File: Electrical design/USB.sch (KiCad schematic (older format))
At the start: 18 parts, among them P501 USB_OTG, Q501 Q_NMOS_GSD, Q502 Q_PMOS_GSD, U501 TPD2E001, U502 MCP73834

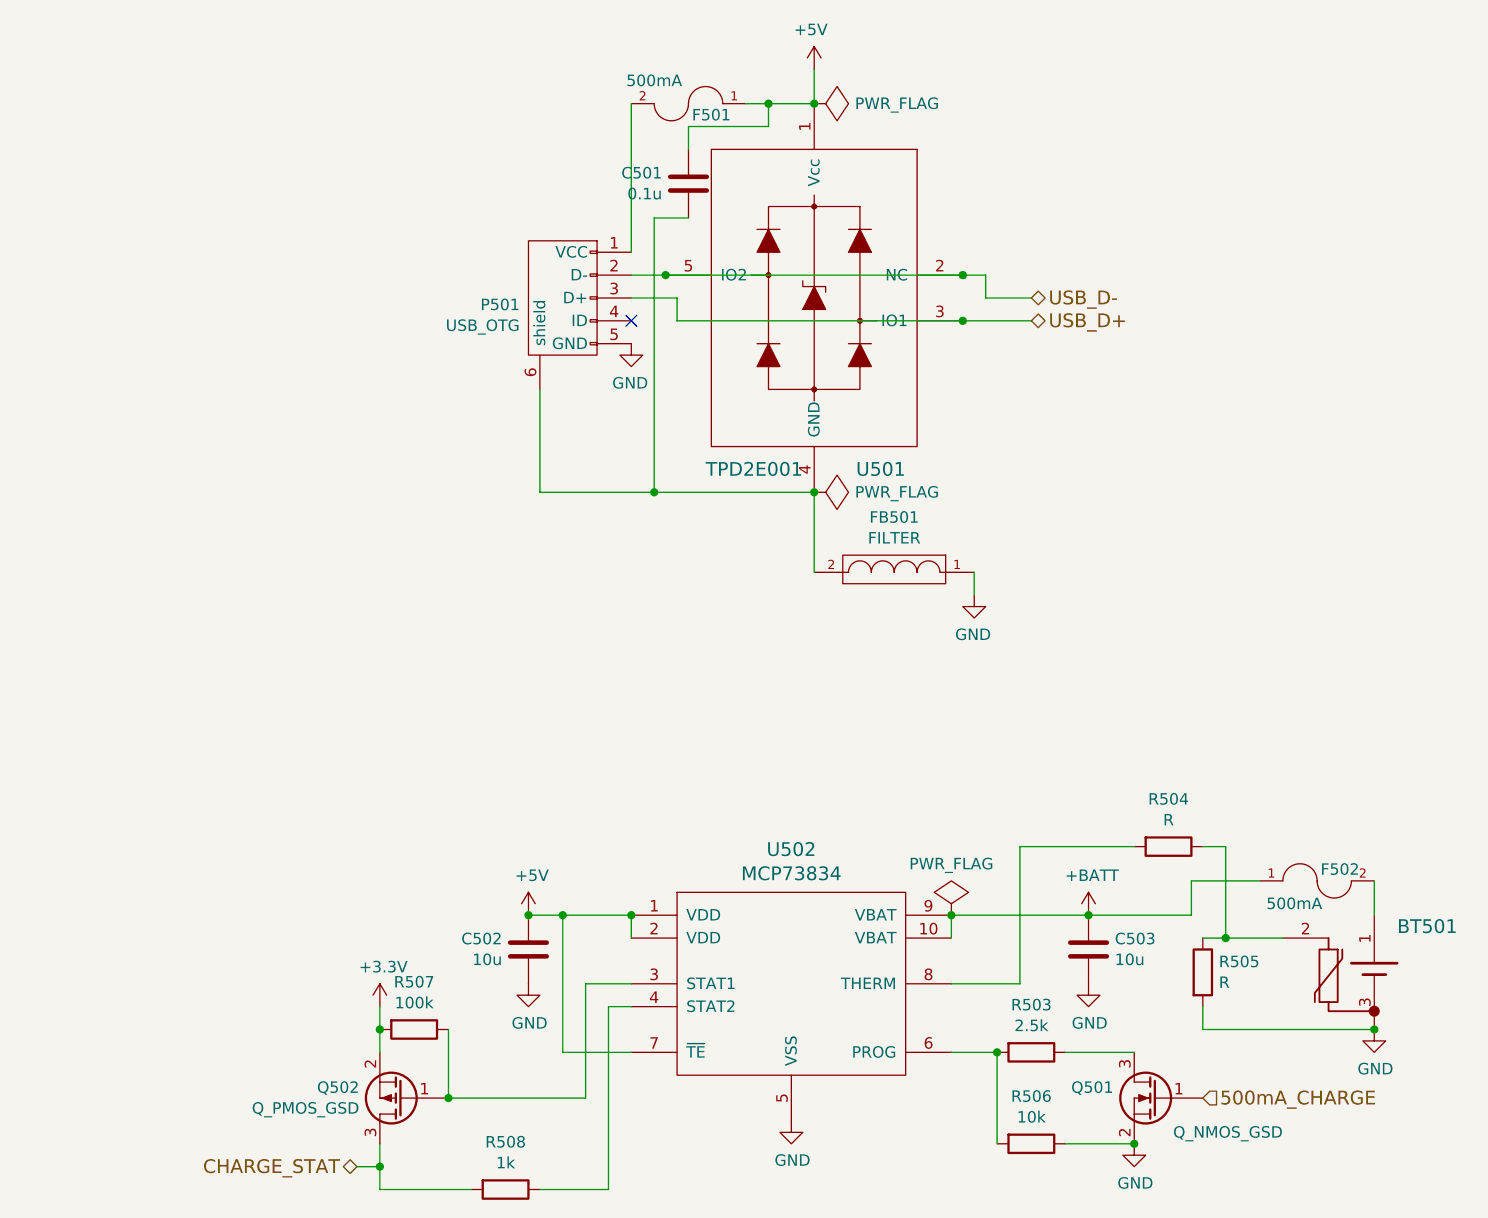
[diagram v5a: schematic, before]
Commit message: Add documentation. Fix some issues found while writing it.
The issues fixed:
Change R245-246 to 1M.
Remove D211-212 and add D213-214.
Power the analog switches from +V_int.
Reconfigure range combination jumpers.
Remove "GND" net.
Correct values of C103-105, and add R106-108 (correcting values of R101-103).
Change +V_int around to be based of +3.3VA instead of +BATT, and clamp to 3.5 V.
Along with above, remove GND rail, mostly replacing with GNDA.
Update PCB for changes.
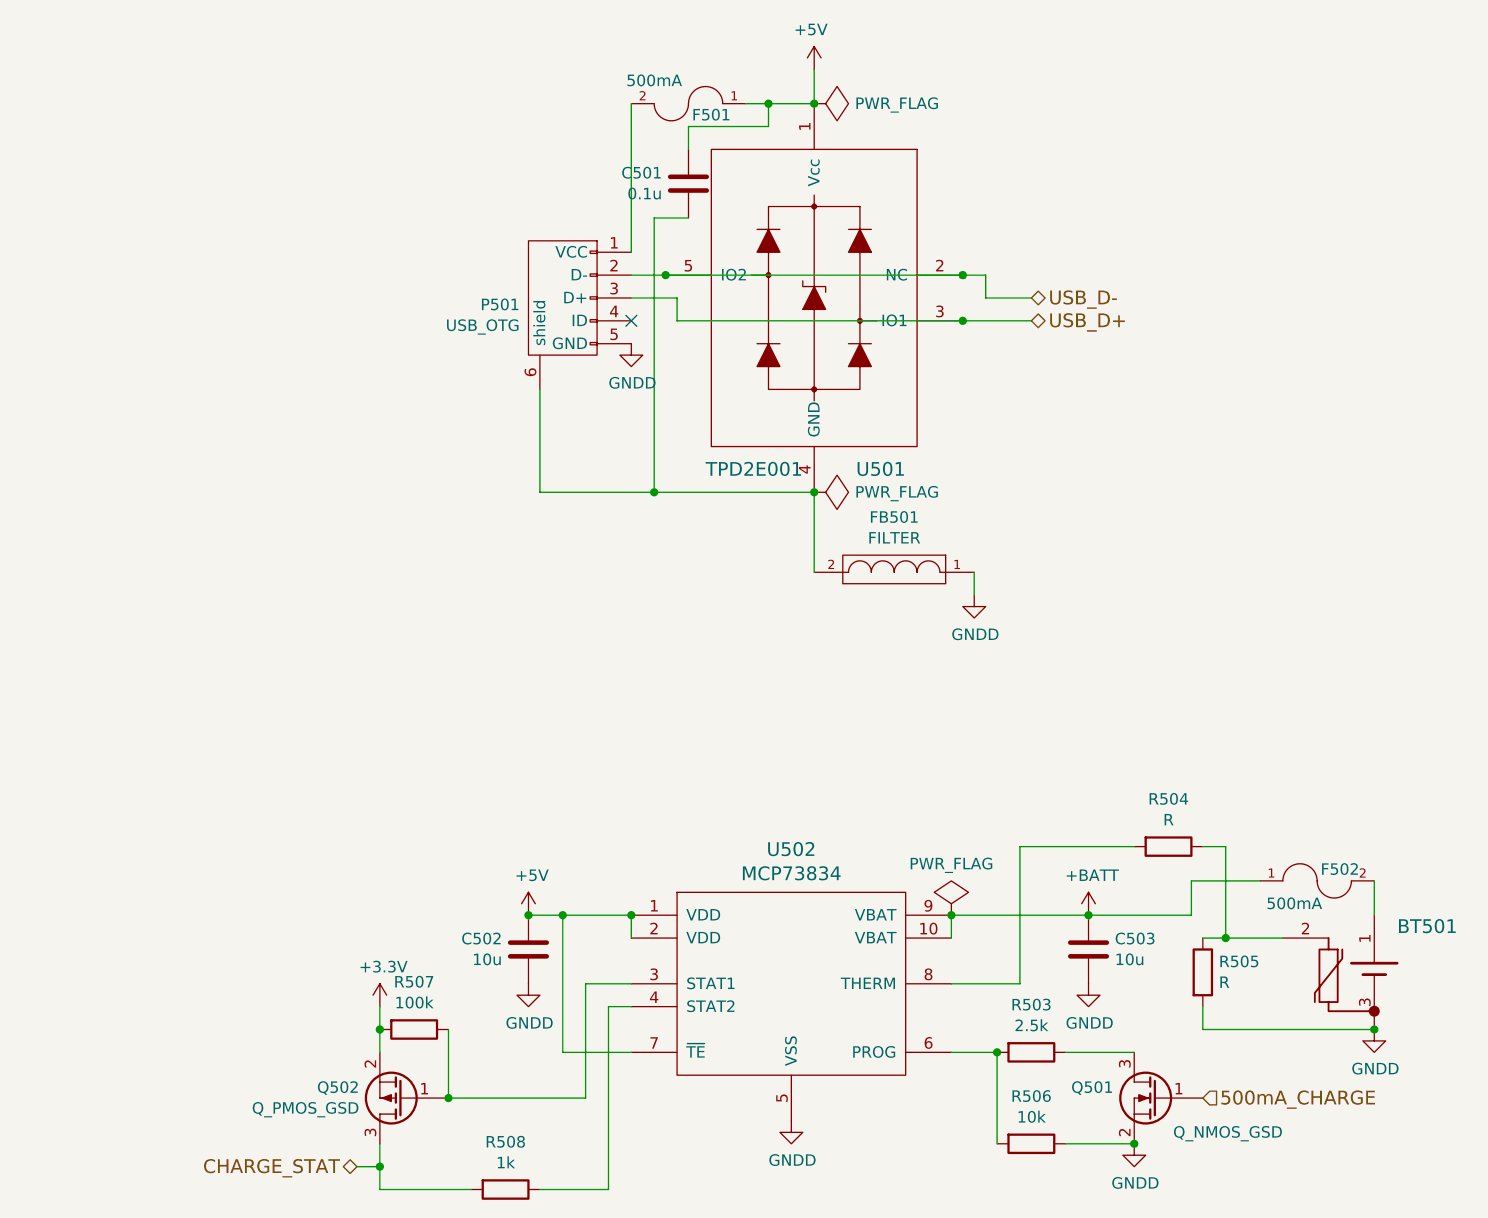
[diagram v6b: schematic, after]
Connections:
- net GND renamed GNDD
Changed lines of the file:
@@
 Sheet 5 5
 Title "USB and charging"
-Date "2016-07-04"
-Rev "0.7"
+Date "2016-07-14"
+Rev "0.8"
 Comp ""
 Comment1 "Licensed under the GNU GPL v3"
@@
 $EndComp
 $Comp
-L +5V #PWR501
+L +5V #PWR064
 U 1 1 57482588
 P 5200 1100
-F 0 "#PWR501" H 5200 950 50  0001 C CNN
+F 0 "#PWR064" H 5200 950 50  0001 C CNN
 F 1 "+5V" H 5215 1273 50  0000 C CNN
 F 2 "" H 5200 1100 50  0000 C CNN
@@
 Text HLabel 6150 2100 2    60   BiDi ~ 0
 USB_D-
-$Comp
-L GND #PWR502
-U 1 1 57482A0F
-P 4400 2300
-F 0 "#PWR502" H 4400 2050 50  0001 C CNN
-F 1 "GND" H 4405 2127 50  0000 C CNN
-F 2 "" H 4400 2300 50  0000 C CNN
-F 3 "" H 4400 2300 50  0000 C CNN
-	1    4400 2300
-	-1   0    0    -1
-$EndComp
 $Comp
 L TPD2E001 U501
@@
 	-1   0    0    -1
 $EndComp
-$Comp
-L GND #PWR503
-U 1 1 57490318
-P 5900 3400
-F 0 "#PWR503" H 5900 3150 50  0001 C CNN
-F 1 "GND" H 5905 3227 50  0000 C CNN
-F 2 "" H 5900 3400 50  0000 C CNN
-F 3 "" H 5900 3400 50  0000 C CNN
-	1    5900 3400
-	-1   0    0    -1
-$EndComp
 NoConn ~ 4400 2200
 Wire Wire Line
@@
 Connection ~ 5850 2000
 $Comp
-L PWR_FLAG #FLG501
+L PWR_FLAG #FLG065
 U 1 1 5767EBE9
 P 5200 1250
-F 0 "#FLG501" H 5200 1345 50  0001 C CNN
+F 0 "#FLG065" H 5200 1345 50  0001 C CNN
 F 1 "PWR_FLAG" V 5200 1428 50  0000 L CNN
 F 2 "" H 5200 1250 50  0000 C CNN
@@
 $EndComp
 $Comp
-L PWR_FLAG #FLG502
+L PWR_FLAG #FLG066
 U 1 1 5767EC78
 P 5200 2950
-F 0 "#FLG502" H 5200 3045 50  0001 C CNN
+F 0 "#FLG066" H 5200 3045 50  0001 C CNN
 F 1 "PWR_FLAG" V 5200 3128 50  0000 L CNN
 F 2 "" H 5200 2950 50  0000 C CNN
@@
 $EndComp
 $Comp
-L +3.3V #PWR508
+L +3.3V #PWR067
 U 1 1 576164CC
 P 3300 5200
-F 0 "#PWR508" H 3300 5050 50  0001 C CNN
+F 0 "#PWR067" H 3300 5050 50  0001 C CNN
 F 1 "+3.3V" H 3315 5373 50  0000 C CNN
 F 2 "" H 3300 5200 50  0000 C CNN
@@
 	5800 5100 6100 5100
 $Comp
-L GND #PWR509
-U 1 1 576152F8
-P 7650 5300
-F 0 "#PWR509" H 7650 5050 50  0001 C CNN
-F 1 "GND" H 7655 5127 50  0000 C CNN
-F 2 "" H 7650 5300 50  0000 C CNN
-F 3 "" H 7650 5300 50  0000 C CNN
-	1    7650 5300
-	1    0    0    -1
-$EndComp
-$Comp
 L Li-Ion_Cell BT501
 U 1 1 57614529
@@
 Wire Wire Line
 	5800 5400 6000 5400
-$Comp
-L GND #PWR510
-U 1 1 57613485
-P 5100 5700
-F 0 "#PWR510" H 5100 5450 50  0001 C CNN
-F 1 "GND" H 5105 5527 50  0000 C CNN
-F 2 "" H 5100 5700 50  0000 C CNN
-F 3 "" H 5100 5700 50  0000 C CNN
-	1    5100 5700
-	1    0    0    -1
-$EndComp
-$Comp
-L GND #PWR507
-U 1 1 5761344A
-P 6400 5100
-F 0 "#PWR507" H 6400 4850 50  0001 C CNN
-F 1 "GND" H 6405 4927 50  0000 C CNN
-F 2 "" H 6400 5100 50  0000 C CNN
-F 3 "" H 6400 5100 50  0000 C CNN
-	1    6400 5100
-	1    0    0    -1
-$EndComp
 Wire Wire Line
 	5800 4900 5800 4800
@@
 	0    1    1    0
 $EndComp
-$Comp
-L GND #PWR506
-U 1 1 57482C8E
-P 3950 5100
-F 0 "#PWR506" H 3950 4850 50  0001 C CNN
-F 1 "GND" H 3955 4927 50  0000 C CNN
-F 2 "" H 3950 5100 50  0000 C CNN
-F 3 "" H 3950 5100 50  0000 C CNN
-	1    3950 5100
-	1    0    0    -1
-$EndComp
 Text HLabel 3200 5900 0    60   3State ~ 0
 CHARGE_STAT
-$Comp
-L GND #PWR511
-U 1 1 57482634
-P 6600 5800
-F 0 "#PWR511" H 6600 5550 50  0001 C CNN
-F 1 "GND" H 6605 5627 50  0000 C CNN
-F 2 "" H 6600 5800 50  0000 C CNN
-F 3 "" H 6600 5800 50  0000 C CNN
-	1    6600 5800
-	1    0    0    -1
-$EndComp
 $Comp
 L R R506
@@
 $EndComp
 $Comp
-L +5V #PWR504
+L +5V #PWR068
 U 1 1 5748259E
 P 3950 4800
-F 0 "#PWR504" H 3950 4650 50  0001 C CNN
+F 0 "#PWR068" H 3950 4650 50  0001 C CNN
 F 1 "+5V" H 3965 4973 50  0000 C CNN
 F 2 "" H 3950 4800 50  0000 C CNN
@@
 $EndComp
 $Comp
-L +BATT #PWR505
+L +BATT #PWR069
 U 1 1 57482544
 P 6400 4800
-F 0 "#PWR505" H 6400 4650 50  0001 C CNN
+F 0 "#PWR069" H 6400 4650 50  0001 C CNN
 F 1 "+BATT" H 6415 4973 50  0000 C CNN
 F 2 "" H 6400 4800 50  0000 C CNN
@@
 	7650 4800 7650 4650
 $Comp
-L PWR_FLAG #FLG503
+L PWR_FLAG #FLG070
 U 1 1 5768BD08
 P 5800 4800
-F 0 "#FLG503" H 5800 4895 50  0001 C CNN
+F 0 "#FLG070" H 5800 4895 50  0001 C CNN
 F 1 "PWR_FLAG" H 5800 5024 50  0000 C CNN
 F 2 "" H 5800 4800 50  0000 C CNN
@@
 	1    0    0    -1
 $EndComp
+$Comp
+L GNDD #PWR071
+U 1 1 57881FC7
+P 7650 5300
+F 0 "#PWR071" H 7650 5050 50  0001 C CNN
+F 1 "GNDD" H 7655 5127 50  0000 C CNN
+F 2 "" H 7650 5300 50  0000 C CNN
+F 3 "" H 7650 5300 50  0000 C CNN
+	1    7650 5300
+	1    0    0    -1
+$EndComp
+$Comp
+L GNDD #PWR072
+U 1 1 57881FFD
+P 6600 5800
+F 0 "#PWR072" H 6600 5550 50  0001 C CNN
+F 1 "GNDD" H 6605 5627 50  0000 C CNN
+F 2 "" H 6600 5800 50  0000 C CNN
+F 3 "" H 6600 5800 50  0000 C CNN
+	1    6600 5800
+	1    0    0    -1
+$EndComp
+$Comp
+L GNDD #PWR073
+U 1 1 57882031
+P 3950 5100
+F 0 "#PWR073" H 3950 4850 50  0001 C CNN
+F 1 "GNDD" H 3955 4927 50  0000 C CNN
+F 2 "" H 3950 5100 50  0000 C CNN
+F 3 "" H 3950 5100 50  0000 C CNN
+	1    3950 5100
+	1    0    0    -1
+$EndComp
+$Comp
+L GNDD #PWR074
+U 1 1 57882065
+P 5100 5700
+F 0 "#PWR074" H 5100 5450 50  0001 C CNN
+F 1 "GNDD" H 5105 5527 50  0000 C CNN
+F 2 "" H 5100 5700 50  0000 C CNN
+F 3 "" H 5100 5700 50  0000 C CNN
+	1    5100 5700
+	1    0    0    -1
+$EndComp
+$Comp
+L GNDD #PWR075
+U 1 1 57882099
+P 4400 2300
+F 0 "#PWR075" H 4400 2050 50  0001 C CNN
+F 1 "GNDD" H 4405 2127 50  0000 C CNN
+F 2 "" H 4400 2300 50  0000 C CNN
+F 3 "" H 4400 2300 50  0000 C CNN
+	1    4400 2300
+	1    0    0    -1
+$EndComp
+$Comp
+L GNDD #PWR076
+U 1 1 578820CD
+P 5900 3400
+F 0 "#PWR076" H 5900 3150 50  0001 C CNN
+F 1 "GNDD" H 5905 3227 50  0000 C CNN
+F 2 "" H 5900 3400 50  0000 C CNN
+F 3 "" H 5900 3400 50  0000 C CNN
+	1    5900 3400
+	1    0    0    -1
+$EndComp
+$Comp
+L GNDD #PWR077
+U 1 1 57882101
+P 6400 5100
+F 0 "#PWR077" H 6400 4850 50  0001 C CNN
+F 1 "GNDD" H 6405 4927 50  0000 C CNN
+F 2 "" H 6400 5100 50  0000 C CNN
+F 3 "" H 6400 5100 50  0000 C CNN
+	1    6400 5100
+	1    0    0    -1
+$EndComp
